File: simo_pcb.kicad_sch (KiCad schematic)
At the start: 1 part

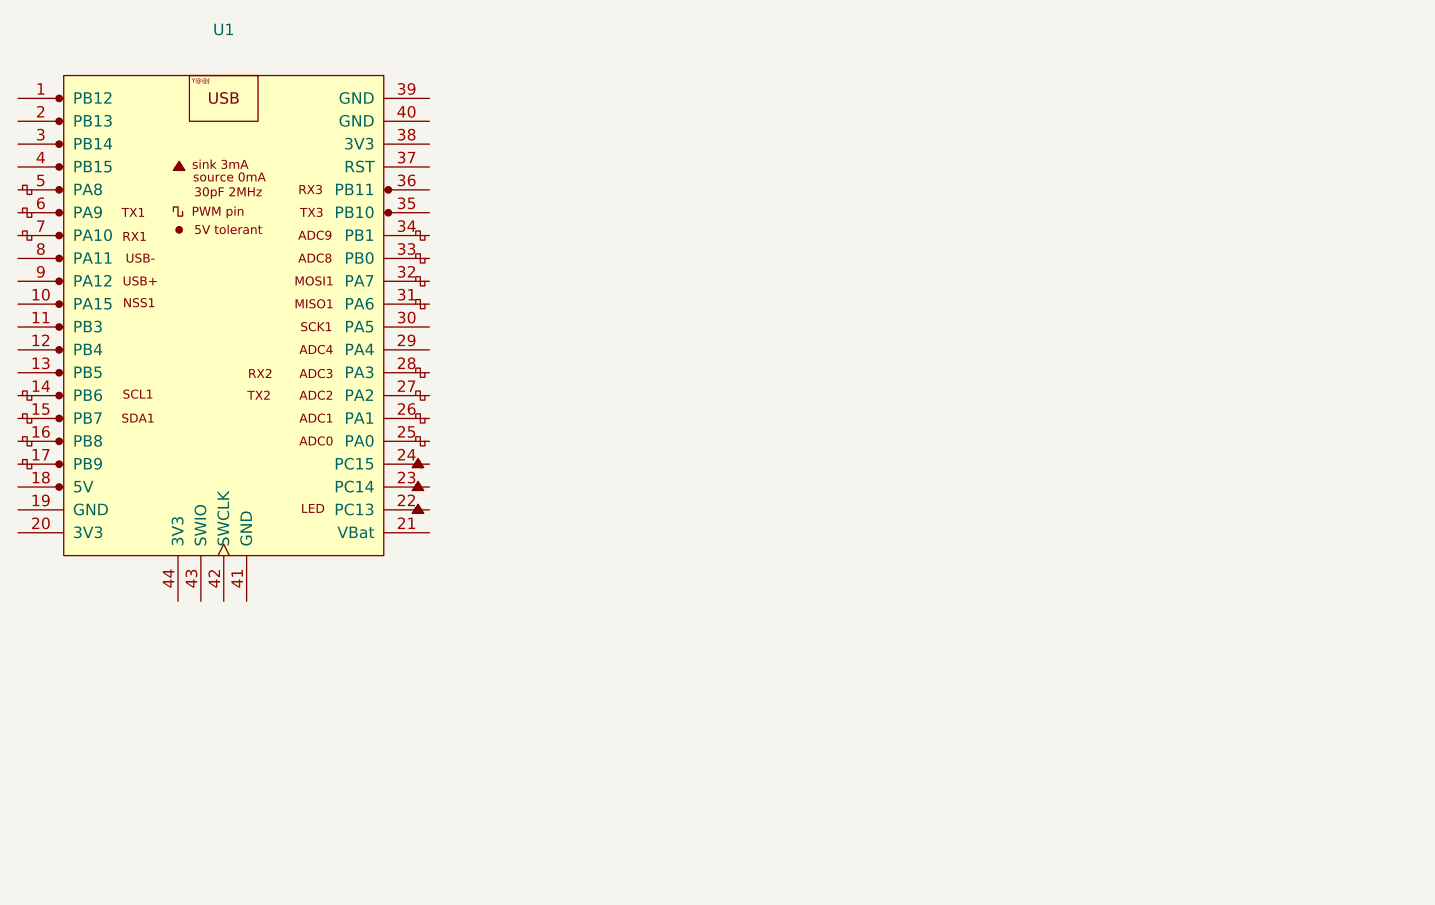
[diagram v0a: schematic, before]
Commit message: modificaciones en elemon_board symbol
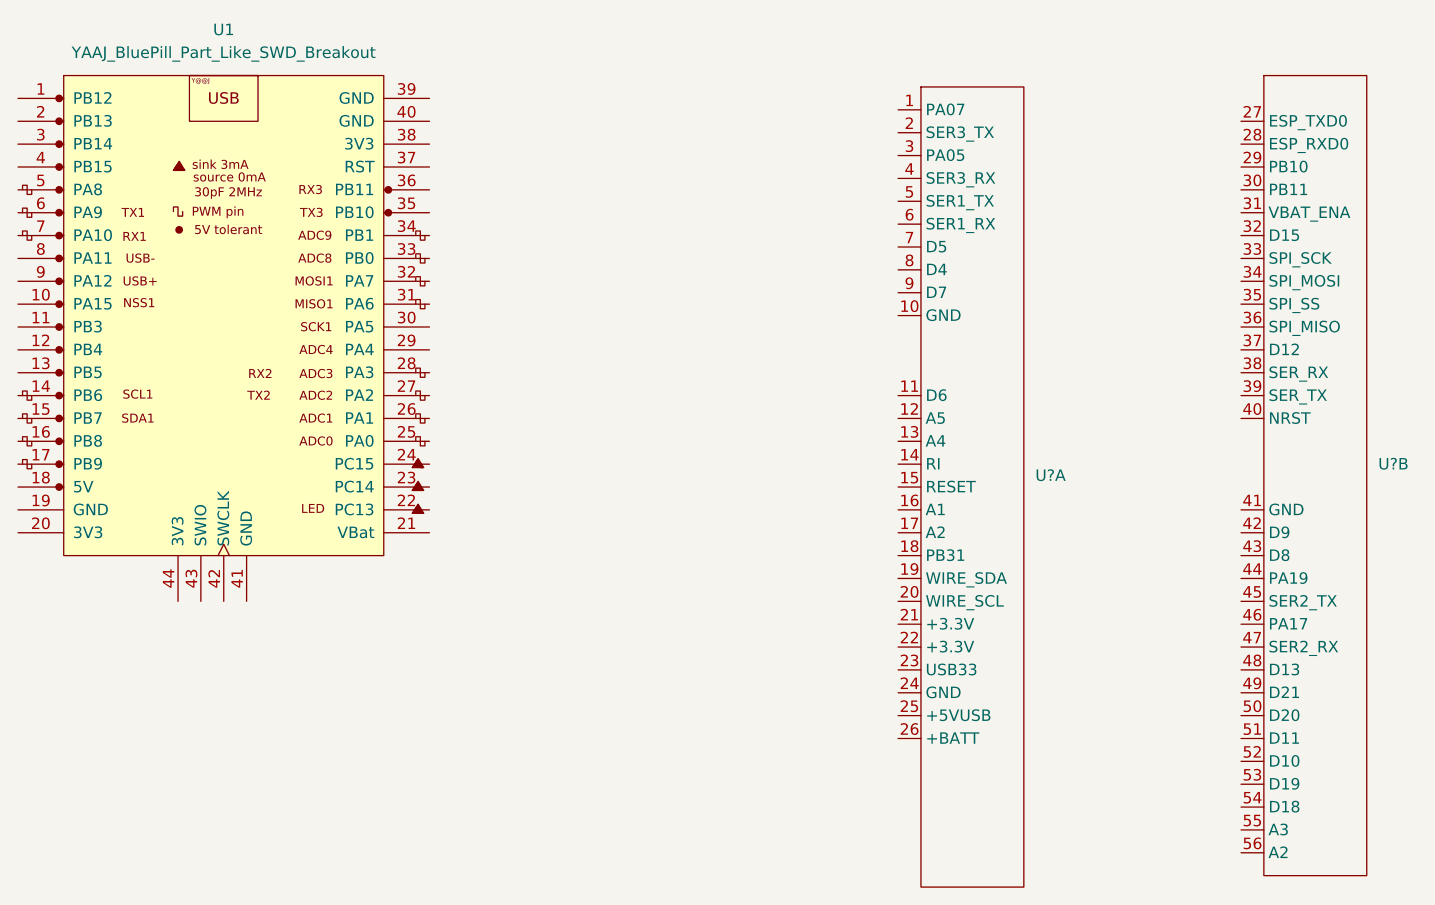
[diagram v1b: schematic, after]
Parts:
- added U? (x2): (no value), symbol simo_board:elemon_board
- U1: value (none) -> YAAJ_BluePill_Part_Like_SWD_Breakout; footprint (none) -> simo:YAAJ_BluePill_SWD_1
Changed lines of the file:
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@@
     (in_bom yes) (on_board yes) (fields_autoplaced)
     (property "Reference" "U1" (id 0) (at 86.36 41.91 0))
-    (property "Value" "" (id 1) (at 86.36 44.45 0))
-    (property "Footprint" "" (id 2) (at 106.68 97.79 0)
+    (property "Value" "YAAJ_BluePill_Part_Like_SWD_Breakout" (id 1) (at 86.36 44.45 0))
+    (property "Footprint" "simo:YAAJ_BluePill_SWD_1" (id 2) (at 106.68 97.79 0)
       (effects (font (size 1.27 1.27)) hide)
     )
@@
     (pin "9")
   )
+  (symbol (lib_id "simo_board:elemon_board") (at 201.93 46.99 0) (unit 2)
+    (in_bom yes) (on_board yes) (fields_autoplaced)
+    (property "Reference" "U?" (id 0) (at 214.63 90.1699 0)
+      (effects (font (size 1.27 1.27)) (justify left))
+    )
+    (property "Value" "" (id 1) (at 214.63 92.7099 0)
+      (effects (font (size 1.27 1.27)) (justify left))
+    )
+    (property "Footprint" "" (id 2) (at 201.93 46.99 0)
+      (effects (font (size 1.27 1.27)) hide)
+    )
+    (property "Datasheet" "" (id 3) (at 201.93 46.99 0)
+      (effects (font (size 1.27 1.27)) hide)
+    )
+    (pin "1")
+    (pin "10")
+    (pin "11")
+    (pin "12")
+    (pin "13")
+    (pin "14")
+    (pin "15")
+    (pin "16")
+    (pin "17")
+    (pin "18")
+    (pin "19")
+    (pin "2")
+    (pin "20")
+    (pin "21")
+    (pin "22")
+    (pin "23")
+    (pin "24")
+    (pin "25")
+    (pin "26")
+    (pin "3")
+    (pin "4")
+    (pin "5")
+    (pin "6")
+    (pin "7")
+    (pin "8")
+    (pin "9")
+    (pin "27")
+    (pin "28")
+    (pin "29")
+    (pin "30")
+    (pin "31")
+    (pin "32")
+    (pin "33")
+    (pin "34")
+    (pin "35")
+    (pin "36")
+    (pin "37")
+    (pin "38")
+    (pin "39")
+    (pin "40")
+    (pin "41")
+    (pin "42")
+    (pin "43")
+    (pin "44")
+    (pin "45")
+    (pin "46")
+    (pin "47")
+    (pin "48")
+    (pin "49")
+    (pin "50")
+    (pin "51")
+    (pin "52")
+    (pin "53")
+    (pin "54")
+    (pin "55")
+    (pin "56")
+  )
+  (symbol (lib_id "simo_board:elemon_board") (at 163.83 48.26 0) (unit 1)
+    (in_bom yes) (on_board yes) (fields_autoplaced)
+    (property "Reference" "U?" (id 0) (at 176.53 91.4399 0)
+      (effects (font (size 1.27 1.27)) (justify left))
+    )
+    (property "Value" "" (id 1) (at 176.53 93.9799 0)
+      (effects (font (size 1.27 1.27)) (justify left))
+    )
+    (property "Footprint" "" (id 2) (at 163.83 48.26 0)
+      (effects (font (size 1.27 1.27)) hide)
+    )
+    (property "Datasheet" "" (id 3) (at 163.83 48.26 0)
+      (effects (font (size 1.27 1.27)) hide)
+    )
+    (pin "1")
+    (pin "10")
+    (pin "11")
+    (pin "12")
+    (pin "13")
+    (pin "14")
+    (pin "15")
+    (pin "16")
+    (pin "17")
+    (pin "18")
+    (pin "19")
+    (pin "2")
+    (pin "20")
+    (pin "21")
+    (pin "22")
+    (pin "23")
+    (pin "24")
+    (pin "25")
+    (pin "26")
+    (pin "3")
+    (pin "4")
+    (pin "5")
+    (pin "6")
+    (pin "7")
+    (pin "8")
+    (pin "9")
+    (pin "27")
+    (pin "28")
+    (pin "29")
+    (pin "30")
+    (pin "31")
+    (pin "32")
+    (pin "33")
+    (pin "34")
+    (pin "35")
+    (pin "36")
+    (pin "37")
+    (pin "38")
+    (pin "39")
+    (pin "40")
+    (pin "41")
+    (pin "42")
+    (pin "43")
+    (pin "44")
+    (pin "45")
+    (pin "46")
+    (pin "47")
+    (pin "48")
+    (pin "49")
+    (pin "50")
+    (pin "51")
+    (pin "52")
+    (pin "53")
+    (pin "54")
+    (pin "55")
+    (pin "56")
+  )
   (sheet_instances
     (path "/" (page "1"))
@@
       (reference "U1") (unit 1) (value "YAAJ_BluePill_Part_Like_SWD_Breakout") (footprint "simo:YAAJ_BluePill_SWD_1")
     )
-  )
+    (path "/67356e78-0efe-482f-a454-ed1826d52ea6"
+      (reference "U?") (unit 1) (value "elemon_board") (footprint "")
+    )
+    (path "/1e823c03-b937-4ab7-abb4-e3fa1b077214"
+      (reference "U?") (unit 2) (value "elemon_board") (footprint "")
+    )
+  )
